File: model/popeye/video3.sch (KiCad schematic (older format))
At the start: 17 parts

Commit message: wip
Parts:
- added 5U1: 74LS04, symbol jt74xx:74LS04
- added unit 2 of 6T1
- added unit 3 of 6T1
- added unit 1 of 6T1
- gave numbers to parts that had none: 2
- renumbered 5L to 5L1, 6T to 6T1, 6U to 6U1, 7L to 7L1, 7M to 7M1, 7N to 7N1, 7P to 7P1, 7R to 7R1, 7S to 7S1, 7T to 7T1, 7U to 7U1, 8P to 8P1, 8S to 8S1, 8T to 8T1, 8U to 8U1
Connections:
- net AD[0]: now also 5U1.3; no longer 7P1.2 (I0a)
- net AD[1]: now also 5U1.11; no longer 7P1.5 (I0b)
- net AD[2]: now also 5U1.13; no longer 7P1.11 (I0d)
- net AD[3]: now also 5U1.5; no longer 7R1.2 (I0a)
- net AD[4]: now also 5U1.9; no longer 7R1.5 (I0b)
- net AD[5]: now also 5U1.1; no longer 7S1.5 (I0b)
- net AT[11]: now also 8S1.18 (CSn), 6T1.1
- net BK[6]: now reaches 8T1.10 (I1d)
- net BK[6]: now also 7U1.9 (Zd), 8P1.16 (D[6]), 8S1.16 (D[6])
- net BK[2]: now reaches 8T1.11 (I0d)
- net BK[2]: now also 7T1.9 (Zd), 8P1.11 (D[2]), 8S1.11 (D[2])
- net BK[7]: now reaches 8T1.13 (I1c)
- net BK[7]: now also 7U1.12 (Zc), 8P1.17 (D[7]), 8S1.17 (D[7])
- net BK[3]: now reaches 8T1.14 (I0c)
- net BK[3]: now also 7T1.12 (Zc), 8P1.13 (D[3]), 8S1.13 (D[3])
- net BK[0]: now reaches 8T1.2 (I0a)
- net BK[0]: now also 7T1.4 (Za), 8P1.9 (D[0]), 8S1.9 (D[0])
- net BK[4]: now reaches 8T1.3 (I1a)
- net BK[4]: now also 7U1.4 (Za), 8P1.14 (D[4]), 8S1.14 (D[4])
- net BK[1]: now reaches 8T1.5 (I0b)
- net BK[1]: now also 7T1.7 (Zb), 8P1.10 (D[1]), 8S1.10 (D[1])
- net BK[5]: now reaches 8T1.6 (I1b)
- net BK[5]: now also 7U1.7 (Zb), 8P1.15 (D[5]), 8S1.15 (D[5])
- net at 7T1.15 (OE): now also 7U1.15 (OE), 6T1.6
- net AT11n: now reaches 8P1.18 (CSn)
- net AT11n: now also 6T1.2
- net DWRBKn: now reaches 8P1.21 (WEn)
- net DWRBKn: now also 8S1.21 (WEn), 6T1.3
- new net: 6T1.4, 6T1.5
- new net ADx[0]: 5U1.4, 7P1.2 (I0a)
- new net ADx[1]: 5U1.10, 7P1.5 (I0b)
- new net ADx[2]: 5U1.12, 7P1.11 (I0d)
- new net ADx[3]: 5U1.6, 7R1.2 (I0a)
- new net ADx[4]: 5U1.8, 7R1.5 (I0b)
- new net ADx[5]: 5U1.2, 7S1.5 (I0b)

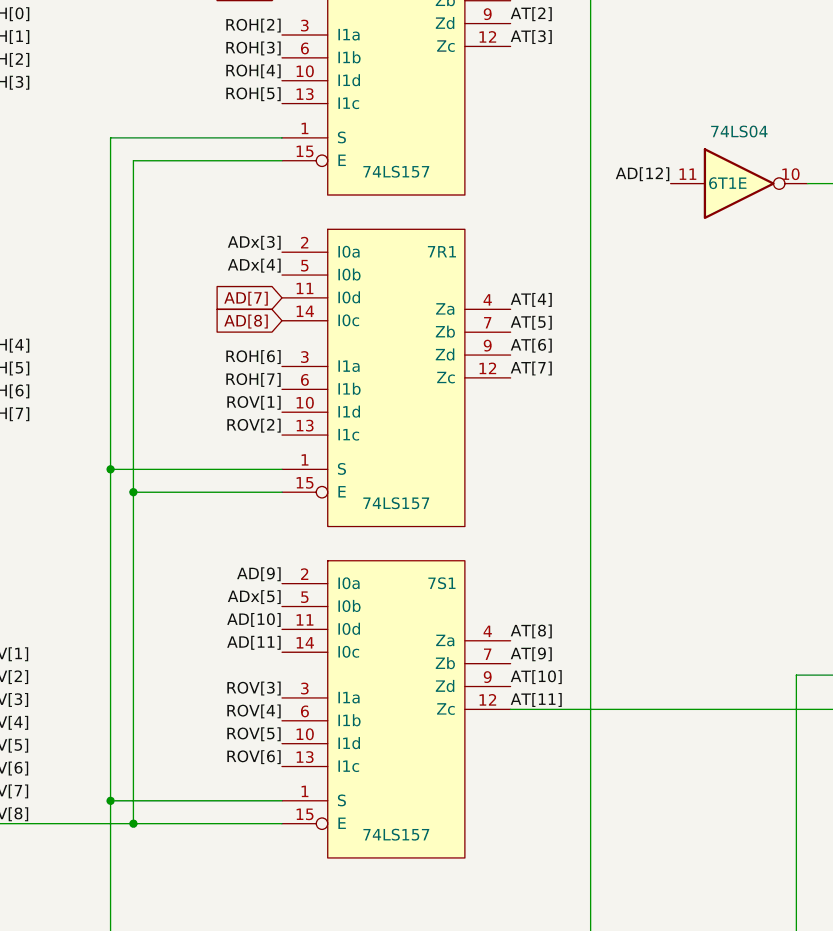
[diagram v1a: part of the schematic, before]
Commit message: Fixed background upside down problem
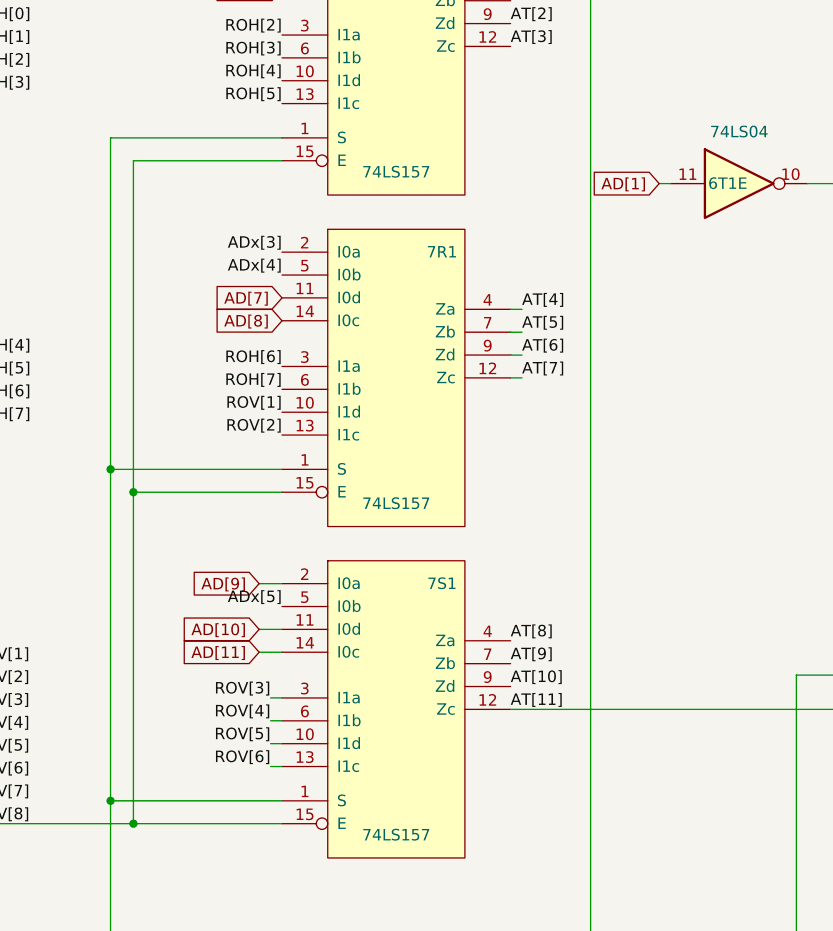
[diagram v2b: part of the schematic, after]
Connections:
- net AD[12] is gone; now on net AD[1]: 6T1.11
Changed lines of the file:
@@
 Text Label 9400 2900 0    50   ~ 0
 AT[3]
-Text Label 9400 4050 0    50   ~ 0
+Text Label 9450 4050 0    50   ~ 0
 AT[4]
-Text Label 9400 4150 0    50   ~ 0
+Text Label 9450 4150 0    50   ~ 0
 AT[5]
-Text Label 9400 4250 0    50   ~ 0
+Text Label 9450 4250 0    50   ~ 0
 AT[6]
-Text Label 9400 4350 0    50   ~ 0
+Text Label 9450 4350 0    50   ~ 0
 AT[7]
 Text Label 9400 5500 0    50   ~ 0
@@
 Text Label 9400 5800 0    50   ~ 0
 AT[11]
-Text Label 8400 5250 2    50   ~ 0
-AD[9]
 Text Label 8400 5350 2    50   ~ 0
 ADx[5]
-Text Label 8400 5450 2    50   ~ 0
-AD[10]
-Text Label 8400 5550 2    50   ~ 0
-AD[11]
 $Comp
 L jt74xx:74LS273 U8
@@
 Text Label 8400 4600 2    50   ~ 0
 ROV[2]
-Text Label 8400 5750 2    50   ~ 0
+Text Label 8350 5750 2    50   ~ 0
 ROV[3]
-Text Label 8400 5850 2    50   ~ 0
+Text Label 8350 5850 2    50   ~ 0
 ROV[4]
-Text Label 8400 5950 2    50   ~ 0
+Text Label 8350 5950 2    50   ~ 0
 ROV[5]
-Text Label 8400 6050 2    50   ~ 0
+Text Label 8350 6050 2    50   ~ 0
 ROV[6]
 Wire Wire Line
@@
 	1    0    0    -1
 $EndComp
-Text Label 10100 3500 2    50   ~ 0
-AD[12]
 Text GLabel 11250 1250 0    50   Input ~ 0
 MEMWR0
@@
 Text Label 13650 2950 2    50   ~ 0
 BK[7]
+Wire Wire Line
+	9400 4050 9450 4050
+Wire Wire Line
+	9450 4150 9400 4150
+Wire Wire Line
+	9400 4250 9450 4250
+Wire Wire Line
+	9450 4350 9400 4350
+Wire Wire Line
+	8350 5750 8400 5750
+Wire Wire Line
+	8400 5850 8350 5850
+Wire Wire Line
+	8350 5950 8400 5950
+Wire Wire Line
+	8400 6050 8350 6050
+Text GLabel 8300 5450 0    50   Input ~ 0
+AD[10]
+Wire Wire Line
+	8300 5450 8400 5450
+Text GLabel 8300 5550 0    50   Input ~ 0
+AD[11]
+Wire Wire Line
+	8300 5550 8400 5550
+Text GLabel 8300 5250 0    50   Input ~ 0
+AD[9]
+Wire Wire Line
+	8300 5250 8400 5250
+Text GLabel 10050 3500 0    50   Input ~ 0
+AD[1]
+Wire Wire Line
+	10050 3500 10100 3500
 $EndSCHEMATC

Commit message: wip
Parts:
- 8P1, 8S1: symbol jt74xx:RAM_2016 -> arcade:RAM_2016
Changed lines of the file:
@@
 $Descr A2 23386 16535
 encoding utf-8
-Sheet 4 4
+Sheet 4 5
 Title ""
 Date ""
@@
 Connection ~ 7650 6850
 $Comp
-L jt74xx:RAM_2016 8P1
+L arcade:RAM_2016 8P1
 U 1 1 5DAADF8C
 P 12200 4550
+AR Path="/5DAADF8C" Ref="8P1"  Part="1"
+AR Path="/5DA6783D/5DAADF8C" Ref="8P1"  Part="1"
 F 0 "8P1" H 12175 5415 50  0000 C CNN
 F 1 "RAM_2016" H 12175 5324 50  0000 C CNN
@@
 $EndComp
 $Comp
-L jt74xx:RAM_2016 8S1
+L arcade:RAM_2016 8S1
 U 1 1 5DAAE0B1
 P 12200 6600
+AR Path="/5DAAE0B1" Ref="8S1"  Part="1"
+AR Path="/5DA6783D/5DAAE0B1" Ref="8S1"  Part="1"
 F 0 "8S1" H 12175 7465 50  0000 C CNN
 F 1 "RAM_2016" H 12175 7374 50  0000 C CNN
